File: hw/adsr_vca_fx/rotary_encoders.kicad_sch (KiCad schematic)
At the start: 6 parts, among them SW1 RotaryEncoder_Switch, SW2 RotaryEncoder_Switch

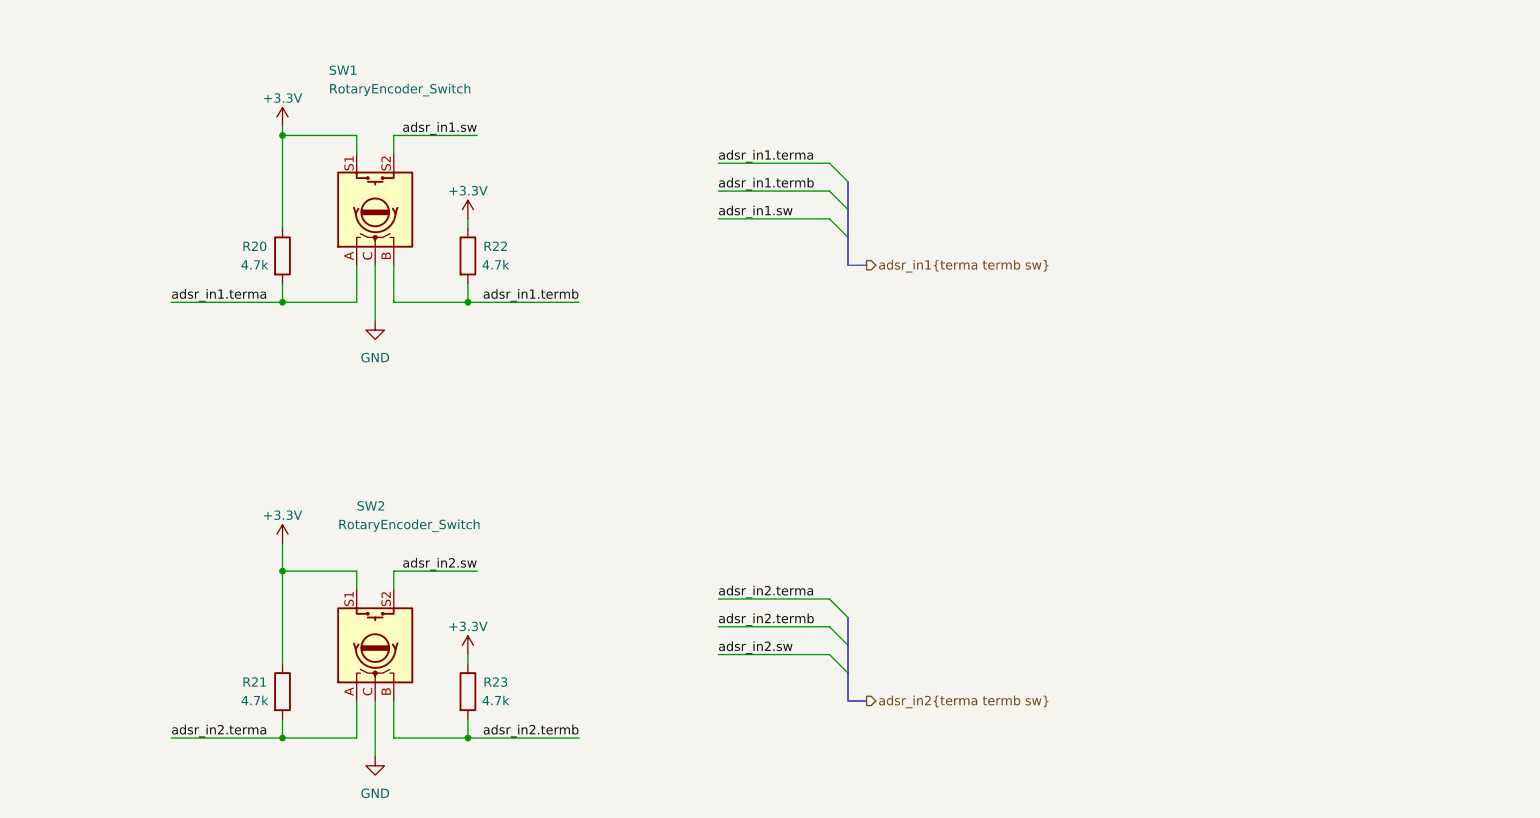
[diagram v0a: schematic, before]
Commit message: modified design into normal/inverted envlope
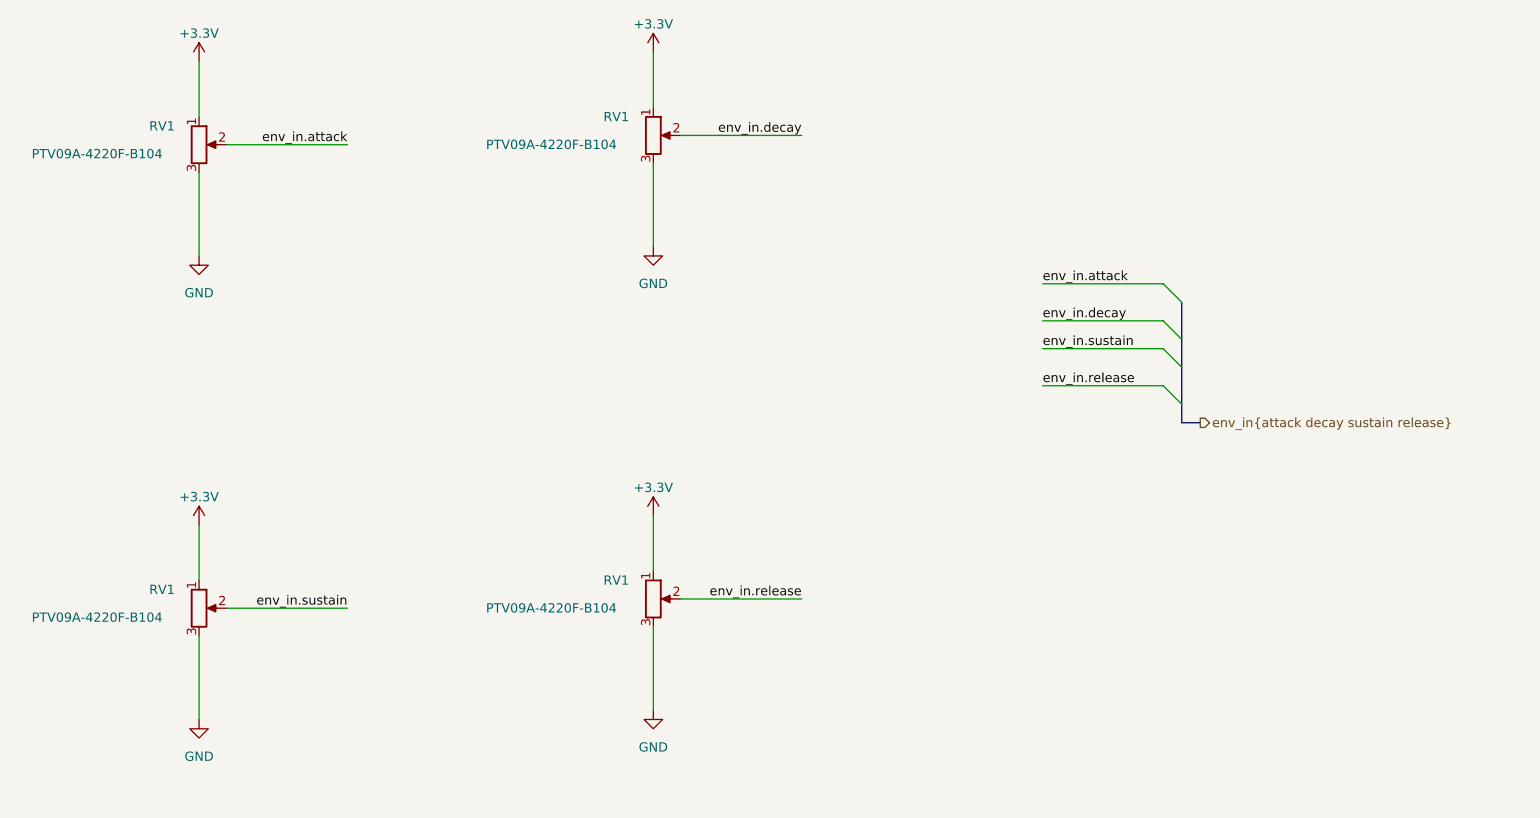
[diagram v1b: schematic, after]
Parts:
- removed R20, R21, R22, R23: 4.7k, Resistor_SMD:R_0805_2012Metric_Pad1.20x1.40mm_HandSolder, symbol Device:R
- removed SW1, SW2: RotaryEncoder_Switch, Rotary_Encoder:RotaryEncoder_Alps_EC12E-Switch_Vertical_H20mm, symbol Device:RotaryEncoder_Switch
- added RV1 (x4): PTV09A-4220F-B104, Potentiometer_THT:Potentiometer_Alpha_RD901F-40-00D_Single_Vertical, symbol Device:R_Potentiometer
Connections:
- net +3.3V: now also RV1.1, RV1.1, RV1.1, RV1.1
- net GND: now also RV1.3, RV1.3, RV1.3, RV1.3
- new net env_in.attack: RV1.2
- new net env_in.decay: RV1.2
- new net env_in.release: RV1.2
- new net env_in.sustain: RV1.2
